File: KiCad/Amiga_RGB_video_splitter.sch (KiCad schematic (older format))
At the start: 23 parts, among them J1 DB23_Female-Connector, J2 DB15_Female_HighDensity_Mount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, J3 KMDGX-9S-BS-1, J4 PJ-320A, J5 MSS22D18 3Pin Slide Toggle Sw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, J6 MSS22D18 3Pin Slide Toggle Sw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, U1 THS7374IPWR, U2 74HCT2G17, U3 74HCT2G14, U4 74LVC1GX04

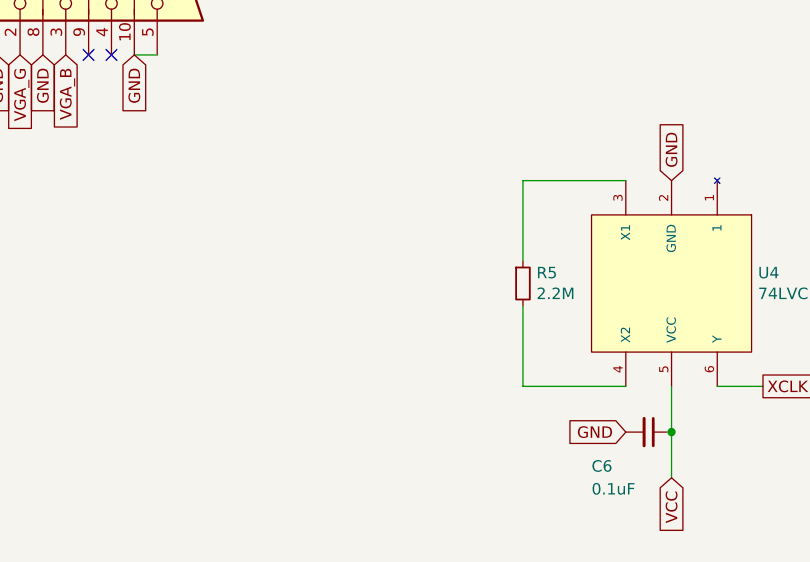
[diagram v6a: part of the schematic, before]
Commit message: Add Y1 crystal to the design
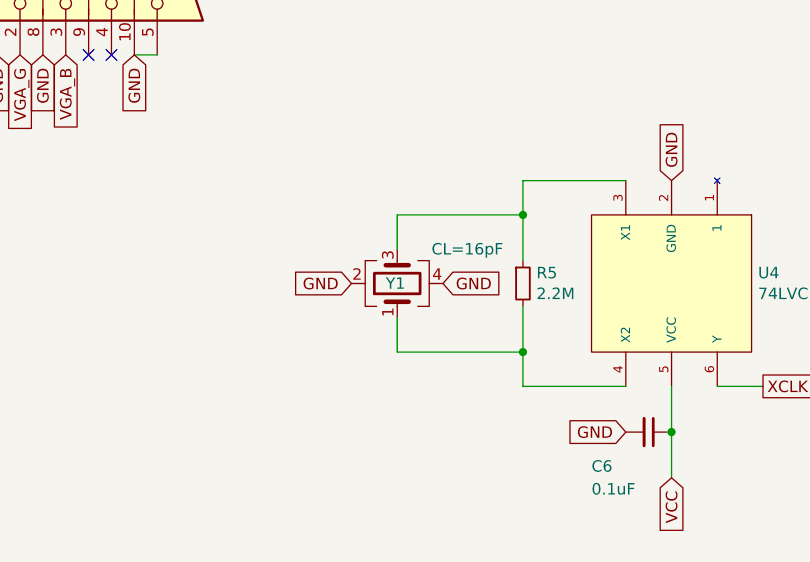
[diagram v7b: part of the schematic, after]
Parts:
- added Y1: CL=16pF, Crystal:Crystal_SMD_SeikoEpson_FA238-4Pin_3.2x2.5mm, symbol Device:Crystal_GND24
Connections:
- net GND: now also Y1.2, Y1.4
- net at R5.1, U4.3 (X1): now also Y1.3
- net at R5.2, U4.4 (X2): now also Y1.1
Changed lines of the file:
@@
 $EndComp
 Wire Wire Line
-	5250 6500 5250 6150
+	5250 6500 5250 6300
 Wire Wire Line
 	5250 6150 5700 6150
@@
 	5700 7050 5250 7050
 Wire Wire Line
-	5250 7050 5250 6700
+	5250 7050 5250 6900
+$Comp
+L Device:Crystal_GND24 Y1
+U 1 1 683ED2B8
+P 4700 6600
+F 0 "Y1" V 4700 6650 50  0000 R CNN
+F 1 "CL=16pF" V 4850 6450 50  0000 R CNN
+F 2 "Crystal:Crystal_SMD_SeikoEpson_FA238-4Pin_3.2x2.5mm" H 4700 6600 50  0001 C CNN
+F 3 "~" H 4700 6600 50  0001 C CNN
+	1    4700 6600
+	0    -1   -1   0
+$EndComp
+Text GLabel 4900 6600 2    50   Input ~ 0
+GND
+Wire Wire Line
+	4700 6450 4700 6300
+Wire Wire Line
+	4700 6300 5250 6300
+Connection ~ 5250 6300
+Wire Wire Line
+	5250 6300 5250 6150
+Wire Wire Line
+	4700 6750 4700 6900
+Wire Wire Line
+	4700 6900 5250 6900
+Connection ~ 5250 6900
+Wire Wire Line
+	5250 6900 5250 6700
+Text GLabel 4500 6600 0    50   Input ~ 0
+GND
 $EndSCHEMATC

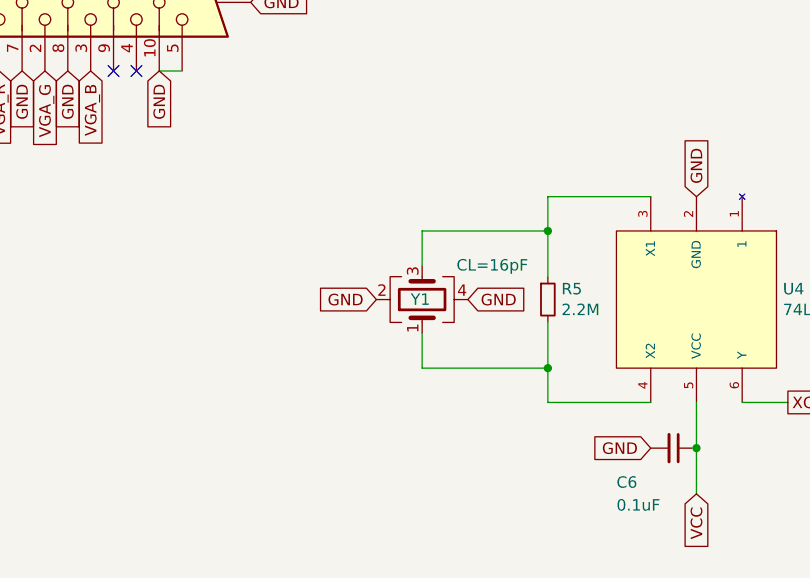
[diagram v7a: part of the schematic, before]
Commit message: Add capacitor C7 and C8, and some silkscreen fixes
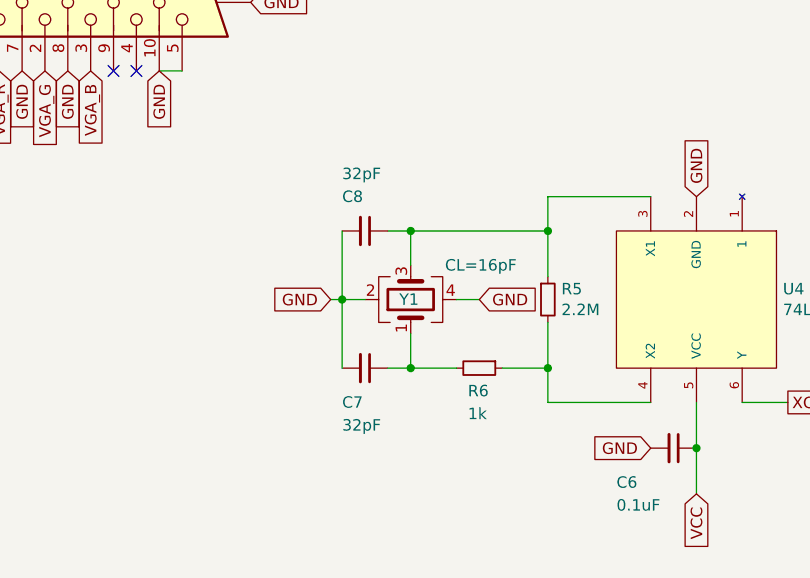
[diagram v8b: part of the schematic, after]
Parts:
- added C7, C8: 32pF, Capacitor_SMD:C_0603_1608Metric_Pad1.08x0.95mm_HandSolder, symbol Device:C_Small
- added R6: 1k, Resistor_SMD:R_0603_1608Metric_Pad0.98x0.95mm_HandSolder, symbol Device:R_Small
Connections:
- net GND: now also C7.2, C8.2
- net at R5.1, U4.3 (X1), Y1.3: now also C8.1
- net at R5.2, U4.4 (X2): now also R6.1; no longer Y1.1
- new net: C7.1, R6.2, Y1.1
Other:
- moved on the sheet: Y1
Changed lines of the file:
@@
 $EndComp
-Wire Wire Line
-	5250 6500 5250 6300
 Wire Wire Line
 	5250 6150 5700 6150
 Wire Wire Line
 	5700 7050 5250 7050
-Wire Wire Line
-	5250 7050 5250 6900
 $Comp
 L Device:Crystal_GND24 Y1
 U 1 1 683ED2B8
-P 4700 6600
-F 0 "Y1" V 4700 6650 50  0000 R CNN
-F 1 "CL=16pF" V 4850 6450 50  0000 R CNN
-F 2 "Crystal:Crystal_SMD_SeikoEpson_FA238-4Pin_3.2x2.5mm" H 4700 6600 50  0001 C CNN
-F 3 "~" H 4700 6600 50  0001 C CNN
-	1    4700 6600
+P 4650 6600
+F 0 "Y1" V 4650 6650 50  0000 R CNN
+F 1 "CL=16pF" V 4800 6450 50  0000 R CNN
+F 2 "Crystal:Crystal_SMD_SeikoEpson_FA238-4Pin_3.2x2.5mm" H 4650 6600 50  0001 C CNN
+F 3 "~" H 4650 6600 50  0001 C CNN
+	1    4650 6600
 	0    -1   -1   0
 $EndComp
-Text GLabel 4900 6600 2    50   Input ~ 0
+Text GLabel 4950 6600 2    50   Input ~ 0
 GND
 Wire Wire Line
-	4700 6450 4700 6300
+	4650 6450 4650 6300
 Wire Wire Line
-	4700 6300 5250 6300
+	4650 6750 4650 6900
+Text GLabel 4300 6600 0    50   Input ~ 0
+GND
+$Comp
+L Device:R_Small R6
+U 1 1 683F6DEA
+P 4950 6900
+F 0 "R6" V 5050 6850 50  0000 L CNN
+F 1 "1k" V 5150 6850 50  0000 L CNN
+F 2 "Resistor_SMD:R_0603_1608Metric_Pad0.98x0.95mm_HandSolder" H 4950 6900 50  0001 C CNN
+F 3 "~" H 4950 6900 50  0001 C CNN
+	1    4950 6900
+	0    1    1    0
+$EndComp
+Wire Wire Line
+	5250 6700 5250 6900
+Wire Wire Line
+	5250 6150 5250 6300
+Wire Wire Line
+	4650 6300 5250 6300
 Connection ~ 5250 6300
 Wire Wire Line
-	5250 6300 5250 6150
+	5250 6300 5250 6500
 Wire Wire Line
-	4700 6750 4700 6900
-Wire Wire Line
-	4700 6900 5250 6900
+	5050 6900 5250 6900
 Connection ~ 5250 6900
 Wire Wire Line
-	5250 6900 5250 6700
-Text GLabel 4500 6600 0    50   Input ~ 0
-GND
+	5250 6900 5250 7050
+Wire Wire Line
+	4850 6900 4650 6900
+$Comp
+L Device:C_Small C8
+U 1 1 68407AAC
+P 4450 6300
+F 0 "C8" V 4300 6200 50  0000 L CNN
+F 1 "32pF" V 4200 6200 50  0000 L CNN
+F 2 "Capacitor_SMD:C_0603_1608Metric_Pad1.08x0.95mm_HandSolder" H 4450 6300 50  0001 C CNN
+F 3 "~" H 4450 6300 50  0001 C CNN
+	1    4450 6300
+	0    1    1    0
+$EndComp
+$Comp
+L Device:C_Small C7
+U 1 1 68409377
+P 4450 6900
+F 0 "C7" V 4600 6800 50  0000 L CNN
+F 1 "32pF" V 4700 6800 50  0000 L CNN
+F 2 "Capacitor_SMD:C_0603_1608Metric_Pad1.08x0.95mm_HandSolder" H 4450 6900 50  0001 C CNN
+F 3 "~" H 4450 6900 50  0001 C CNN
+	1    4450 6900
+	0    1    1    0
+$EndComp
+Wire Wire Line
+	4550 6300 4650 6300
+Connection ~ 4650 6300
+Wire Wire Line
+	4550 6900 4650 6900
+Connection ~ 4650 6900
+Wire Wire Line
+	4950 6600 4850 6600
+Wire Wire Line
+	4350 6300 4350 6600
+Wire Wire Line
+	4450 6600 4350 6600
+Connection ~ 4350 6600
+Wire Wire Line
+	4350 6600 4350 6900
+Wire Wire Line
+	4350 6600 4300 6600
 $EndSCHEMATC
